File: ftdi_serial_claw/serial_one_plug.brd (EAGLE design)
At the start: 21.9 x 26.7 mm, 6 parts

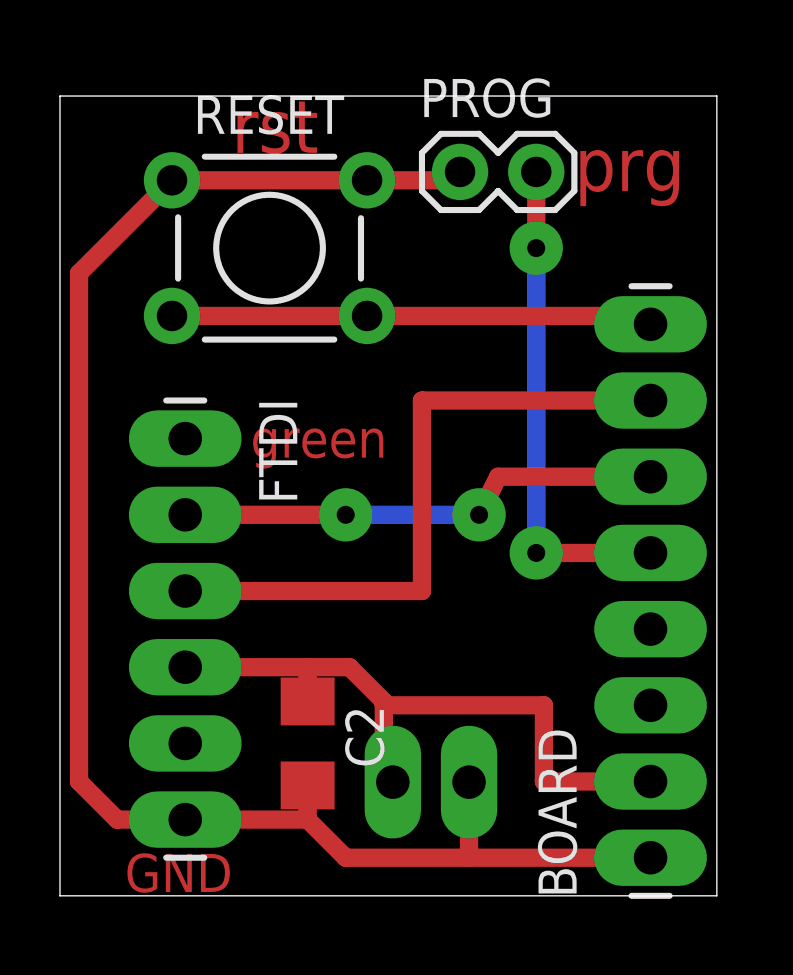
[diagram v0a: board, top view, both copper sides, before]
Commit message: added inliner, more top text
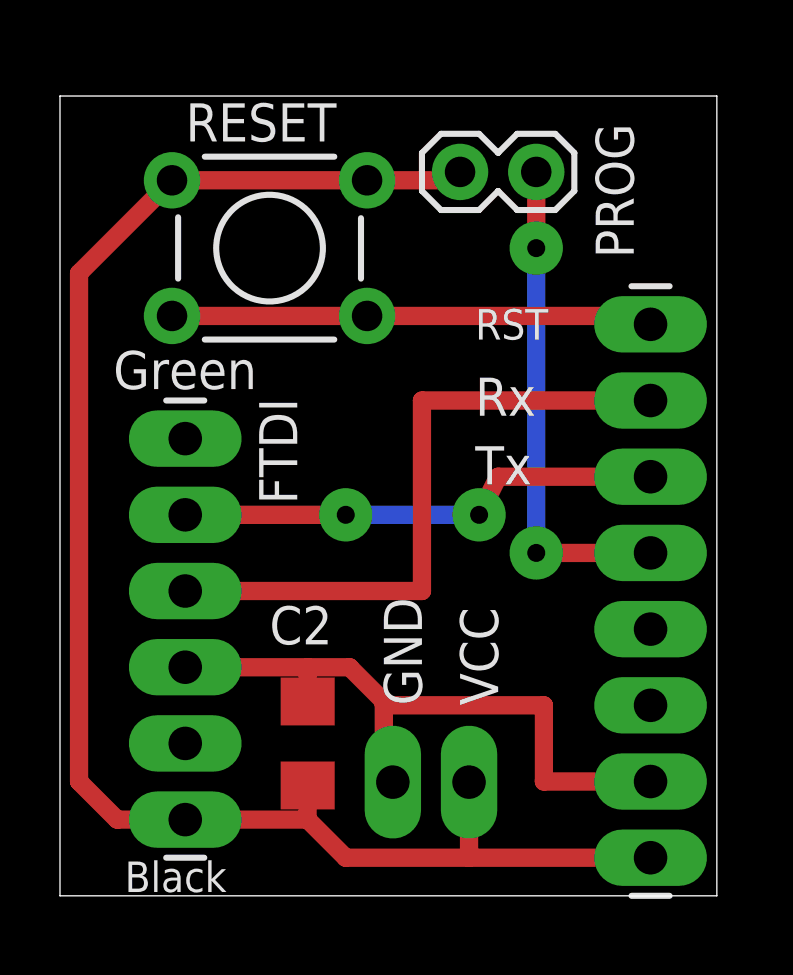
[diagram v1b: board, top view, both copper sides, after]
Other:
- board text added: "Black"
- board text added: "Green"
- board text added: "RST"
- board text added: "Rx"
- board text added: "Tx"
- board text added: "VCC"
- board text removed: "green"
- board text removed: "prg"
- board text removed: "rst"
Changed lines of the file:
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@@
 <wire x1="19.99" y1="25.39" x2="-1.905" y2="25.39" width="0" layer="20"/>
 <wire x1="-1.905" y1="25.39" x2="-1.905" y2="-1.27" width="0" layer="20"/>
-<text x="15.24" y="22.225" size="1.778" layer="1">prg</text>
-<text x="3.81" y="23.495" size="1.778" layer="1">rst</text>
-<text x="4.445" y="13.335" size="1.27" layer="1">green</text>
-<text x="0.254" y="-1.143" size="1.27" layer="1">GND</text>
+<text x="-0.127" y="15.621" size="1.27" layer="25">Green</text>
+<text x="0.254" y="-1.143" size="1.016" layer="25">Black</text>
+<text x="12.7" y="5.08" size="1.27" layer="25" rot="R90">VCC</text>
+<text x="10.16" y="5.08" size="1.27" layer="25" rot="R90">GND</text>
+<text x="11.938" y="17.272" size="1.016" layer="25">RST</text>
+<text x="11.938" y="14.732" size="1.27" layer="25">Rx</text>
+<text x="11.938" y="12.446" size="1.27" layer="25">Tx</text>
 </plain>
 <attributes>
@@
 <element name="FTDI" library="SparkFun-Connectors" package="1X06_LONGPADS" value="" x="2.27" y="13.97" rot="R270"/>
 <element name="POWER_RAIL" library="SparkFun-Connectors" package="1X02_LONGPADS" value="M02PTH3" x="11.73" y="2.52" rot="R180"/>
-<element name="BOARD" library="SparkFun-Connectors" package="1X08_LONGPADS" value="" x="17.78" y="0" rot="R90"/>
-<element name="RESET" library="SparkFun-Electromechanical" package="TACTILE-PTH" value="" x="5.08" y="20.32"/>
-<element name="PROG" library="SparkFun-Connectors" package="1X02" value="M02PTH" x="11.43" y="22.86"/>
-<element name="C2" library="rcl" package="C1206" value="0.1 uF" x="6.35" y="3.81" rot="R270"/>
+<element name="BOARD" library="SparkFun-Connectors" package="1X08_LONGPADS" value="" x="17.78" y="0" smashed="yes" rot="R90">
+<attribute name="VALUE" x="21.59" y="-1.27" size="1.27" layer="27" rot="R90"/>
+</element>
+<element name="RESET" library="SparkFun-Electromechanical" package="TACTILE-PTH" value="" x="5.08" y="20.32" smashed="yes">
+<attribute name="NAME" x="2.286" y="23.876" size="1.27" layer="25" ratio="10"/>
+</element>
+<element name="PROG" library="SparkFun-Connectors" package="1X02" value="M02PTH" x="11.43" y="22.86" smashed="yes">
+<attribute name="NAME" x="17.2212" y="19.9898" size="1.27" layer="25" ratio="10" rot="R90"/>
+</element>
+<element name="C2" library="rcl" package="C1206" value="0.1 uF" x="6.35" y="3.81" smashed="yes" rot="R270">
+<attribute name="NAME" x="5.08" y="7.112" size="1.27" layer="25"/>
+</element>
 </elements>
 <signals>
